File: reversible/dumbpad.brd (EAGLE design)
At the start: 97 x 78.5 mm, 47 parts

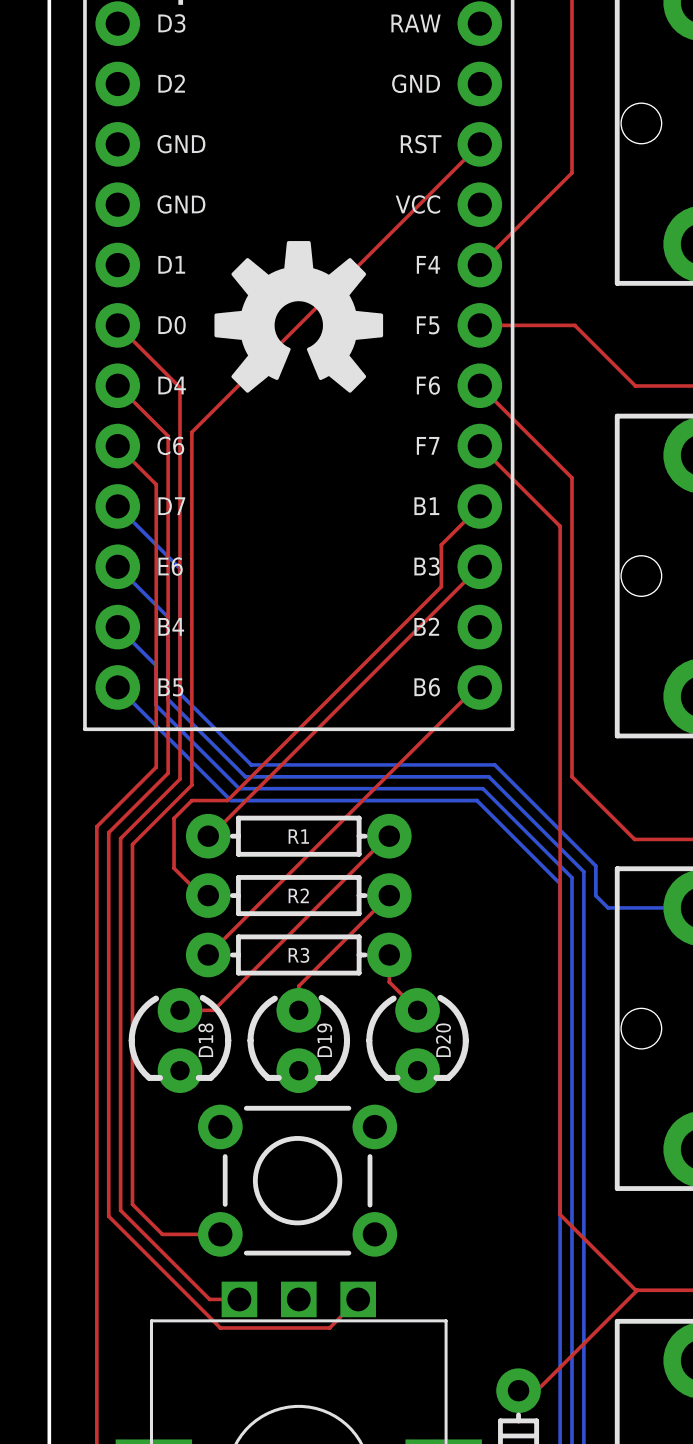
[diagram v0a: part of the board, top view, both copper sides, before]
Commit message: matching reversible version encoder pins to combo
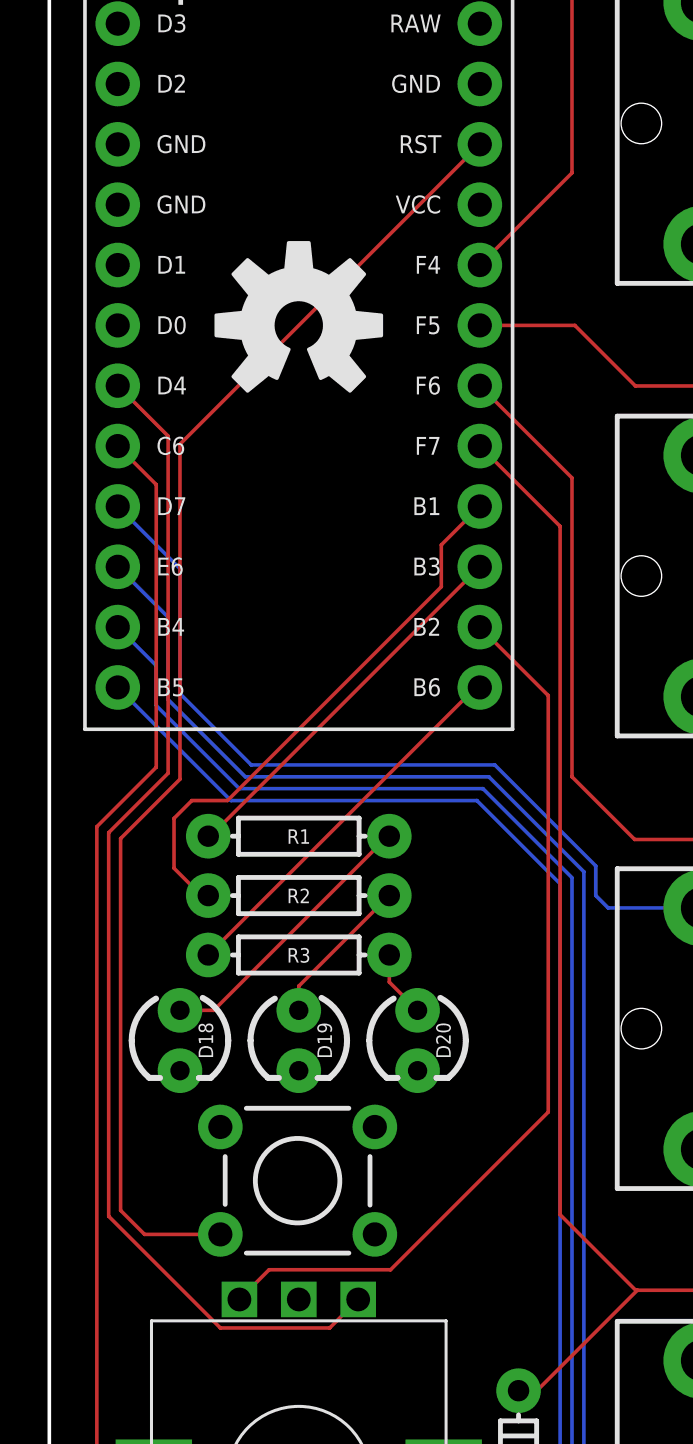
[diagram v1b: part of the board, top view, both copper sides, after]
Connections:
- net ENCODER_L1: now also B1.14; no longer B1.6
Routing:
- net ENCODER_L1: track 45.9 -> 37.9 mm
- net RESET: track 54.9 -> 55.8 mm
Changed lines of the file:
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@@
 </signal>
 <signal name="ENCODER_L1">
-<contactref element="B1" pad="6"/>
-<wire x1="5.5" y1="40.4" x2="5.5" y2="56.88" width="0.1524" layer="1"/>
-<wire x1="5.5" y1="56.88" x2="2.88" y2="59.5" width="0.1524" layer="1"/>
 <contactref element="RE1" pad="B"/>
-<wire x1="8" y1="18.5" x2="6.75" y2="18.5" width="0.1524" layer="1"/>
-<wire x1="6.75" y1="18.5" x2="3" y2="22.25" width="0.1524" layer="1"/>
-<wire x1="3" y1="37.9" x2="5.5" y2="40.4" width="0.1524" layer="1"/>
-<wire x1="3" y1="22.25" x2="3" y2="37.9" width="0.1524" layer="1"/>
+<contactref element="B1" pad="14"/>
+<wire x1="8" y1="18.5" x2="9.25" y2="19.75" width="0.1524" layer="1"/>
+<wire x1="14.36416875" y1="19.75" x2="21" y2="26.38583125" width="0.1524" layer="1"/>
+<wire x1="21" y1="43.92" x2="18.12" y2="46.8" width="0.1524" layer="1"/>
+<wire x1="9.25" y1="19.75" x2="14.36416875" y2="19.75" width="0.1524" layer="1"/>
+<wire x1="21" y1="26.38583125" x2="21" y2="43.92" width="0.1524" layer="1"/>
 </signal>
 <signal name="ROW0">
@@
 <contactref element="B1" pad="22"/>
 <contactref element="S17" pad="2"/>
-<wire x1="6" y1="55" x2="18.12" y2="67.12" width="0.1524" layer="1"/>
-<wire x1="6" y1="40.15" x2="3.5" y2="37.65" width="0.1524" layer="1"/>
-<wire x1="6" y1="40.15" x2="6" y2="55" width="0.1524" layer="1"/>
-<wire x1="4.7606" y1="21.2394" x2="7.1988" y2="21.2394" width="0.1524" layer="1"/>
-<wire x1="3.5" y1="37.65" x2="3.5" y2="22.5" width="0.1524" layer="1"/>
-<wire x1="3.5" y1="22.5" x2="4.7606" y2="21.2394" width="0.1524" layer="1"/>
+<wire x1="5.5" y1="54.5" x2="18.12" y2="67.12" width="0.1524" layer="1"/>
+<wire x1="5.5" y1="40.4" x2="3" y2="37.9" width="0.1524" layer="1"/>
+<wire x1="5.5" y1="40.4" x2="5.5" y2="54.5" width="0.1524" layer="1"/>
+<wire x1="4.0106" y1="21.2394" x2="7.1988" y2="21.2394" width="0.1524" layer="1"/>
+<wire x1="3" y1="37.9" x2="3" y2="22.25" width="0.1524" layer="1"/>
+<wire x1="3" y1="22.25" x2="4.0106" y2="21.2394" width="0.1524" layer="1"/>
 </signal>
 <signal name="COL4">
